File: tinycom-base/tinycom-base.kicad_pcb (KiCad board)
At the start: 2 copper layers, 45.2 x 45.2 mm, 37 parts, among them J1 MICRO_SD_HINGE, P1 CONN_02X10, P2 CONN_02X10, P3 USB_A, P4 USB_OTG, U1 SY8008BAAC, U2 SY8008BAAC, U3 SY8008BAAC, U4 RTL8188, U5 rainsun-antenna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

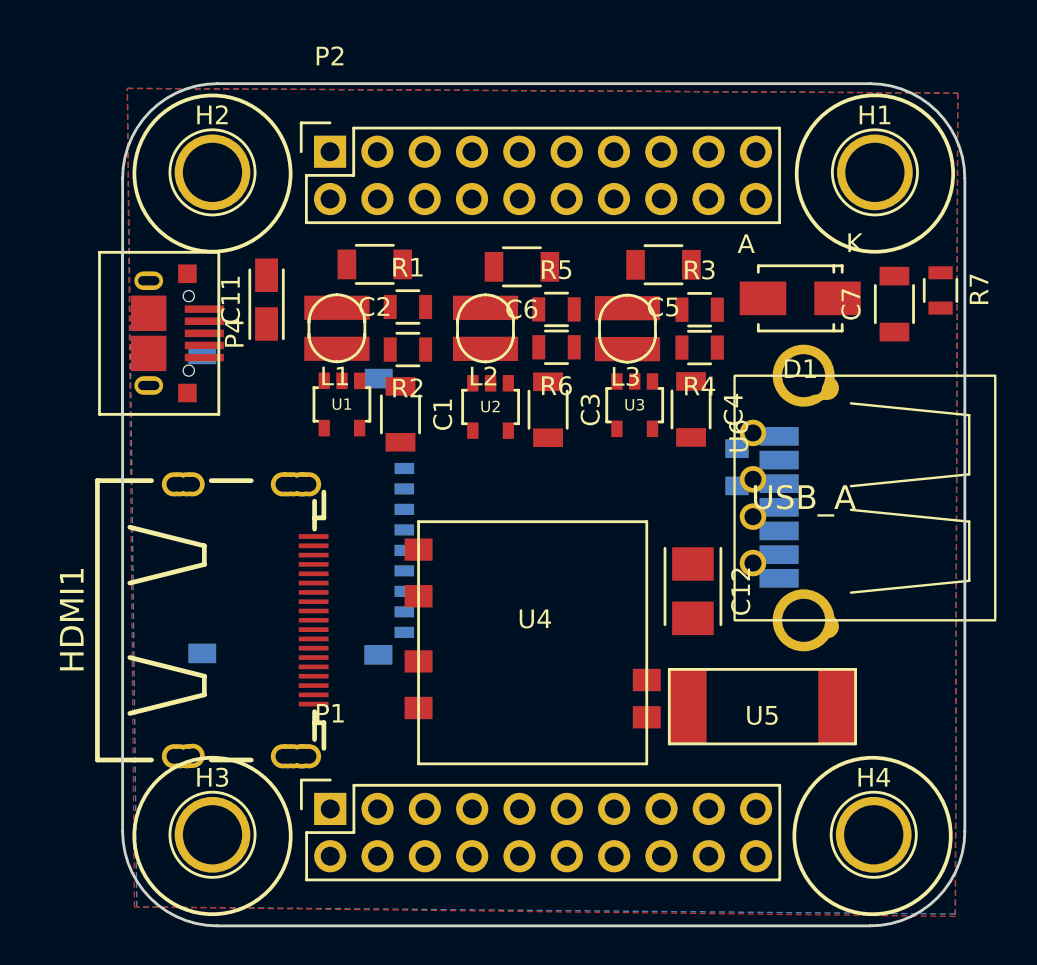
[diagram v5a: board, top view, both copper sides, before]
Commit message: before change a20 connectors
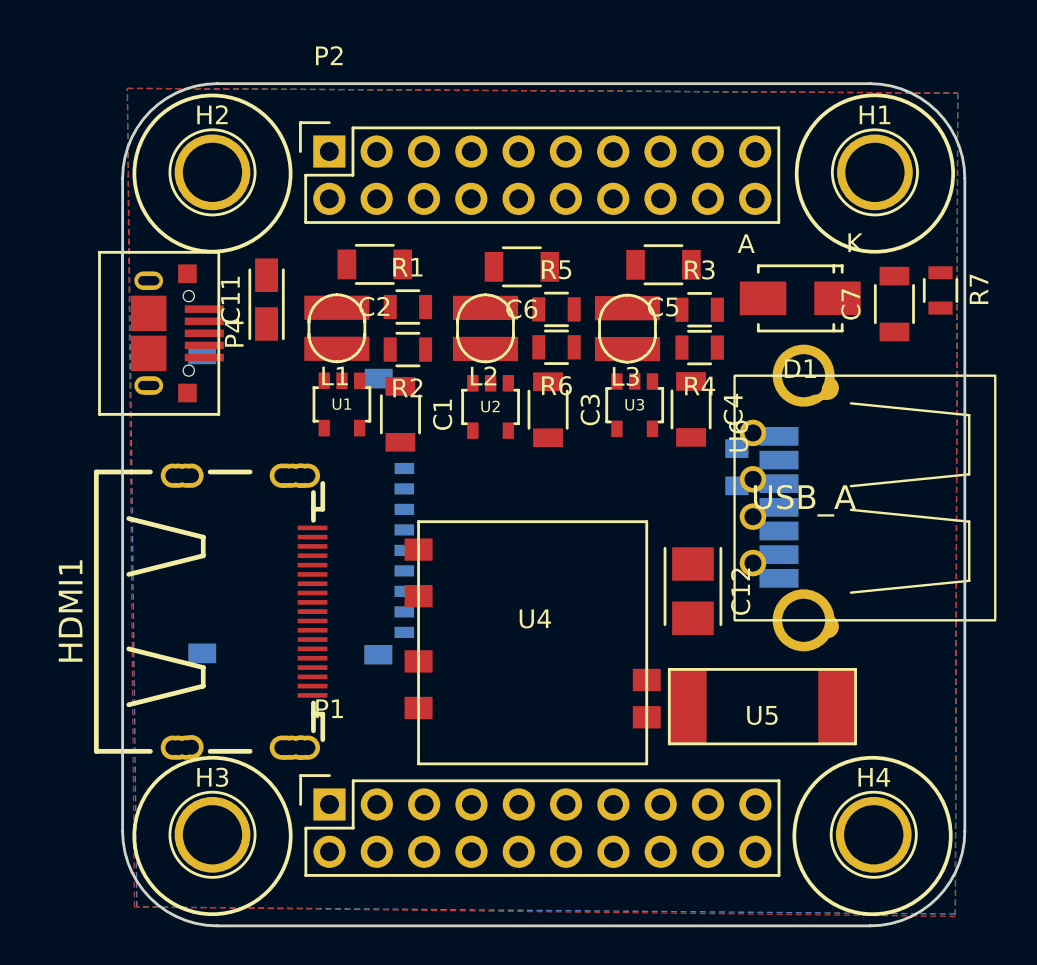
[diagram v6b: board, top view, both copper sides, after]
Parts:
- moved HDMI1 0.47 mm to (129.1, 107.6)
- moved P1 0.24 mm to (135.6, 117.9)
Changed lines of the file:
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@@
   (general
     (links 106)
-    (no_connects 83)
+    (no_connects 75)
     (area 124.384999 79.172999 169.747001 124.535001)
     (thickness 1.6)
@@
   )
   (module tinycom:HDMI-SWM-19 (layer F.Cu)
-    (at 129.167 108.057 90)
+    (at 129.107 107.592 90)
     (descr "PADOVETE OT 1.6X0.28 STAVAT NA 1.6X0.25")
     (tags "PADOVETE OT 1.6X0.28 STAVAT NA 1.6X0.25")
@@
   )
   (module Socket_Strips:Socket_Strip_Straight_2x10 (layer F.Cu)
-    (at 135.607 118.182)
+    (at 135.567 117.942)
     (descr "Through hole socket strip")
     (tags "socket strip")
@@
   )
   (module Socket_Strips:Socket_Strip_Straight_2x10 (layer F.Cu)
-    (at 135.597 82.902)
+    (at 135.557 82.892)
     (descr "Through hole socket strip")
     (tags "socket strip")

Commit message: start route base board
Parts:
- moved U5 5.71 mm to (164.5, 113.4)
- moved C8 4.44 mm to (153.1, 100.7)
- moved U6 2.80 mm to (173.6, 101.4)
- turned C11 to 270 degrees
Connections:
- P2 pad 14: (no net) -> SATA_TXP
- P2 pad 16: (no net) -> SATA_TXM
- P2 pad 18: (no net) -> SATA_RXP
- P2 pad 20: (no net) -> SATA_RXM
- U6 pad 1: (no net) -> GND
- U6 pad 2: (no net) -> SATA_RXM
- U6 pad 3: (no net) -> SATA_RXP
- U6 pad 4: (no net) -> GND
- U6 pad 5: (no net) -> SATA_TXM
- U6 pad 6: (no net) -> SATA_TXP
- U6 pad 7: (no net) -> GND
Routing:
- net UDM0: track 0.00 -> 45.0 mm
- net UDP1: track 0.00 -> 40.6 mm
- net HHPD: track 0.00 -> 40.6 mm
- net UDM1: track 0.00 -> 39.3 mm
- net UDP0: track 0.00 -> 38.4 mm
- net VCC_30: track 0.00 -> 35.3 mm
- net HSDA: track 0.00 -> 33.8 mm
- net HCSL: track 0.00 -> 29.1 mm
- net UDM2: track 0.00 -> 28.6 mm
- net SATA_TXM: track 0.00 -> 26.3 mm
- net SDC0_D1: track 0.00 -> 26.2 mm
- net HCEC: track 0.00 -> 26.1 mm
- net SATA_TXP: track 0.00 -> 26.1 mm
- net SDC0_D0: track 0.00 -> 23.7 mm
- net HTXCN: track 0.00 -> 23.4 mm
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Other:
- net class Default: trace_width 0.2 -> 0.4
